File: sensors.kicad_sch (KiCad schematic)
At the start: 2 parts, among them M4 Module-vr-max9924-0.1, M5 Module-knock-0.2

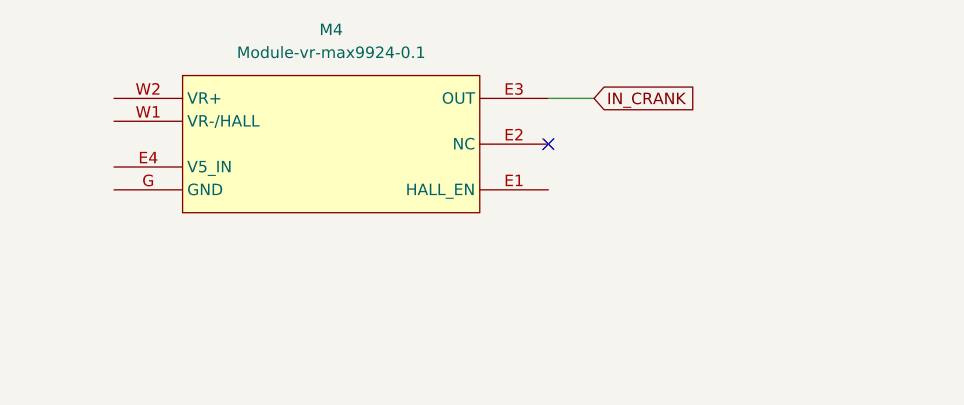
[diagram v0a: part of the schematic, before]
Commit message: Implementing some inputs and outputs
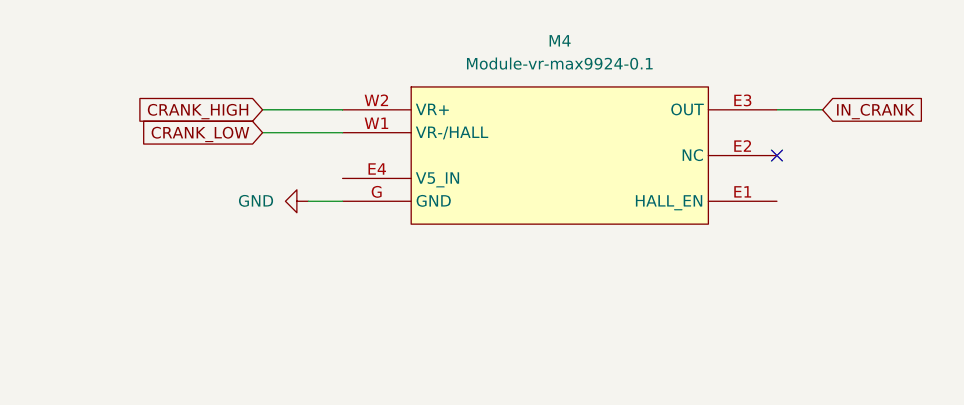
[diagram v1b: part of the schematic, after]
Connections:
- net GND: now also M4.G (GND)
- net CRANK_LOW: now reaches M4.W1 (VR-/HALL)
- net CRANK_HIGH: now reaches M4.W2 (VR+)
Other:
- moved on the sheet: M4
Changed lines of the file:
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@@
 	(paper "A4")
 	(no_connect
-		(at 77.47 46.99)
-	)
-	(wire
-		(pts
-			(xy 77.47 41.91) (xy 82.55 41.91)
+		(at 102.87 48.26)
+	)
+	(wire
+		(pts
+			(xy 102.87 43.18) (xy 107.95 43.18)
+		)
+		(stroke
+			(width 0)
+			(type default)
+		)
+	)
+	(wire
+		(pts
+			(xy 45.72 43.18) (xy 54.61 43.18)
+		)
+		(stroke
+			(width 0)
+			(type default)
+		)
+	)
+	(wire
+		(pts
+			(xy 50.8 53.34) (xy 54.61 53.34)
 		)
 		(stroke
@@
 	(wire
 		(pts
+			(xy 45.72 45.72) (xy 54.61 45.72)
+		)
+		(stroke
+			(width 0)
+			(type default)
+		)
+	)
+	(wire
+		(pts
 			(xy 92.71 120.65) (xy 102.87 120.65)
 		)
@@
 		)
 	)
+	(global_label "CRANK_LOW"
+		(shape input)
+		(at 45.72 45.72 180)
+		(fields_autoplaced yes)
+		(effects
+			(font
+				(size 1.27 1.27)
+			)
+			(justify right)
+		)
+		(property "Intersheetrefs" "${INTERSHEET_REFS}"
+			(at 31.7281 45.72 0)
+			(effects
+				(font
+					(size 1.27 1.27)
+				)
+				(justify right)
+				(hide yes)
+			)
+		)
+	)
 	(global_label "RAW_KNOCK"
 		(shape input)
@@
 	(global_label "IN_CRANK"
 		(shape input)
-		(at 82.55 41.91 0)
+		(at 107.95 43.18 0)
 		(fields_autoplaced yes)
 		(effects
@@
 		)
 		(property "Intersheetrefs" "${INTERSHEET_REFS}"
-			(at 94.6672 41.91 0)
+			(at 120.0672 43.18 0)
 			(effects
 				(font
@@
 				)
 				(justify left)
+				(hide yes)
+			)
+		)
+	)
+	(global_label "CRANK_HIGH"
+		(shape input)
+		(at 45.72 43.18 180)
+		(fields_autoplaced yes)
+		(effects
+			(font
+				(size 1.27 1.27)
+			)
+			(justify right)
+		)
+		(property "Intersheetrefs" "${INTERSHEET_REFS}"
+			(at 31.0023 43.18 0)
+			(effects
+				(font
+					(size 1.27 1.27)
+				)
+				(justify right)
 				(hide yes)
 			)
@@
 	(symbol
 		(lib_id "vr-max9924:Module-vr-max9924-0.1")
-		(at 36.83 39.37 0)
+		(at 62.23 40.64 0)
 		(unit 1)
 		(exclude_from_sim no)
@@
 		(fields_autoplaced yes)
 		(property "Reference" "M4"
-			(at 53.34 34.29 0)
+			(at 78.74 35.56 0)
 			(effects
 				(font
@@
 		)
 		(property "Value" "Module-vr-max9924-0.1"
-			(at 53.34 36.83 0)
+			(at 78.74 38.1 0)
 			(effects
 				(font
@@
 		)
 		(property "Footprint" "0.3:vr-max9924"
-			(at 62.23 38.1 0)
+			(at 87.63 39.37 0)
 			(effects
 				(font
@@
 		)
 		(property "Datasheet" ""
-			(at 36.83 39.37 0)
+			(at 62.23 40.64 0)
 			(effects
 				(font
@@
 		)
 		(property "Description" ""
-			(at 36.83 39.37 0)
+			(at 62.23 40.64 0)
 			(effects
 				(font
@@
 					(unit 1)
 				)
+			)
+		)
+	)
+	(symbol
+		(lib_id "power:GND")
+		(at 50.8 53.34 270)
+		(unit 1)
+		(exclude_from_sim no)
+		(in_bom yes)
+		(on_board yes)
+		(dnp no)
+		(fields_autoplaced yes)
+		(property "Reference" "#PWR023"
+			(at 44.45 53.34 0)
+			(effects
+				(font
+					(size 1.27 1.27)
+				)
+				(hide yes)
+			)
+		)
+		(property "Value" "GND"
+			(at 46.99 53.3399 90)
+			(effects
+				(font
+					(size 1.27 1.27)
+				)
+				(justify right)
+			)
+		)
+		(property "Footprint" ""
+			(at 50.8 53.34 0)
+			(effects
+				(font
+					(size 1.27 1.27)
+				)
+				(hide yes)
+			)
+		)
+		(property "Datasheet" ""
+			(at 50.8 53.34 0)
+			(effects
+				(font
+					(size 1.27 1.27)
+				)
+				(hide yes)
+			)
+		)
+		(property "Description" "Power symbol creates a global label with name \"GND\" , ground"
+			(at 50.8 53.34 0)
+			(effects
+				(font
+					(size 1.27 1.27)
+				)
+				(hide yes)
+			)
+		)
+		(pin "1"
+		)
+		(instances
+			(project ""
+				(path "/83409e39-90d0-4c85-be2e-bd292bea7c12/c21a1b91-ddb8-4e22-b099-7bd7440ec482"
+					(reference "#PWR023")
+					(unit 1)
+				)

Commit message: trying out a layout and routing
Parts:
- added M6: Module-knock-0.2, hellen_knock:knock, symbol knock:Module-knock-0.2
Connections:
- net GND: now also M6.E2 (GND)
- net MCU_KNOCK renamed MCU_KNOCK_F
- net RAW_KNOCK renamed RAW_KNOCK_F
- new net MCU_KNOCK_R: M6.E3 (OUT_KNOCK)
- new net RAW_KNOCK_R: M6.W1 (IN_KNOCK)
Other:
- moved on the sheet: M5

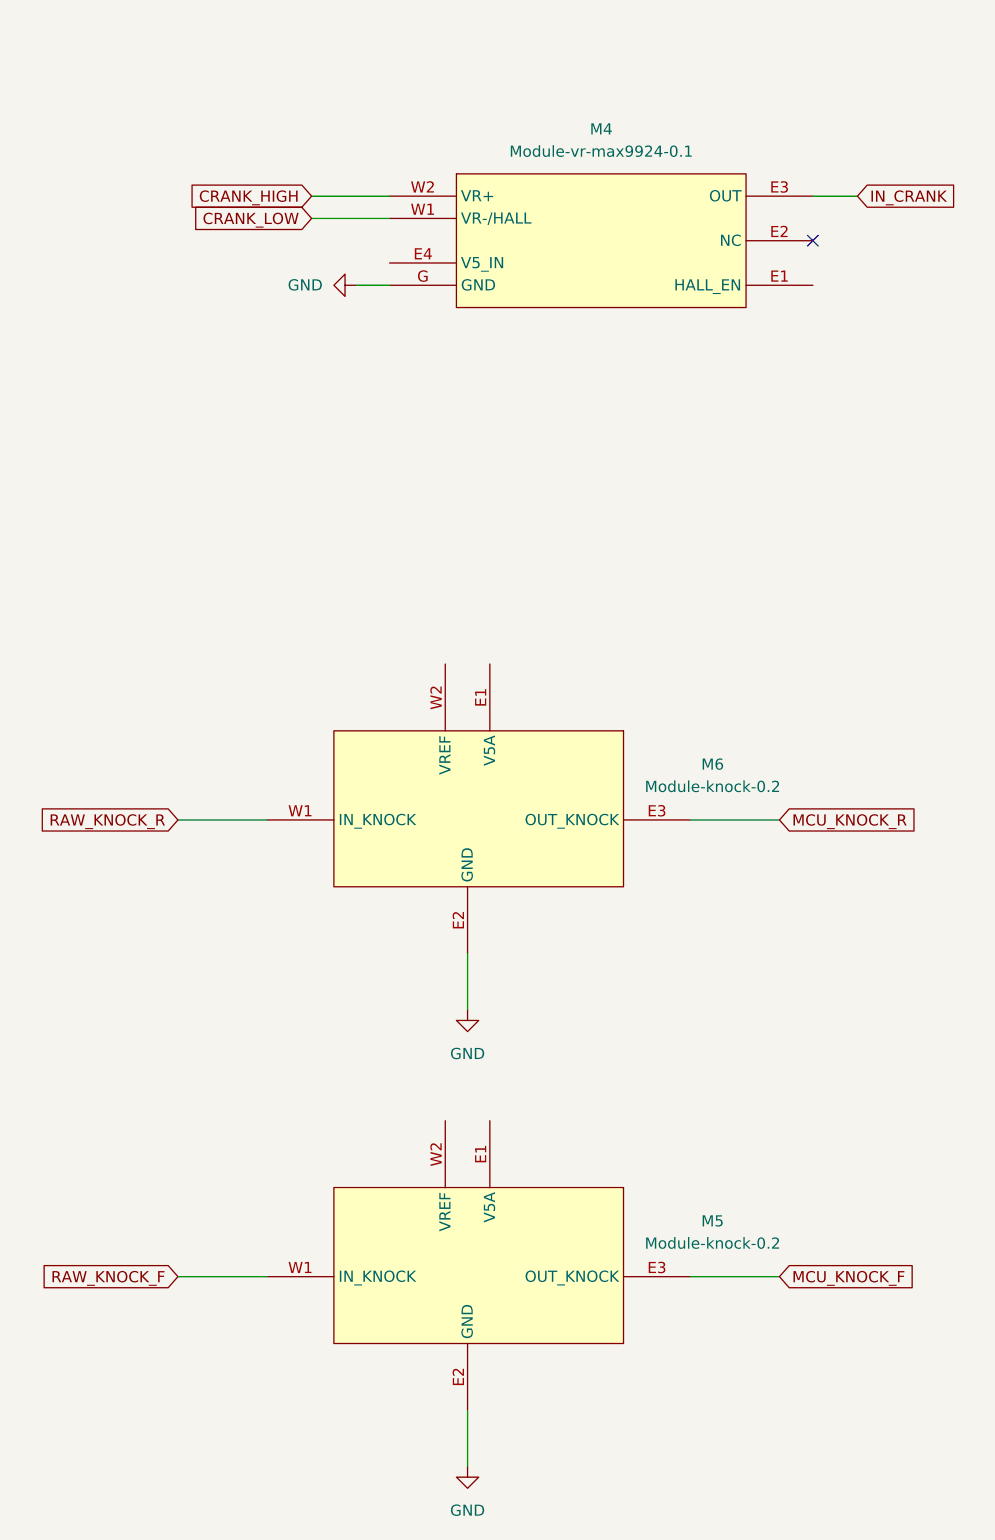
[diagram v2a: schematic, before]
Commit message: adding most remaining outputs and sensors like vvt, cam etc
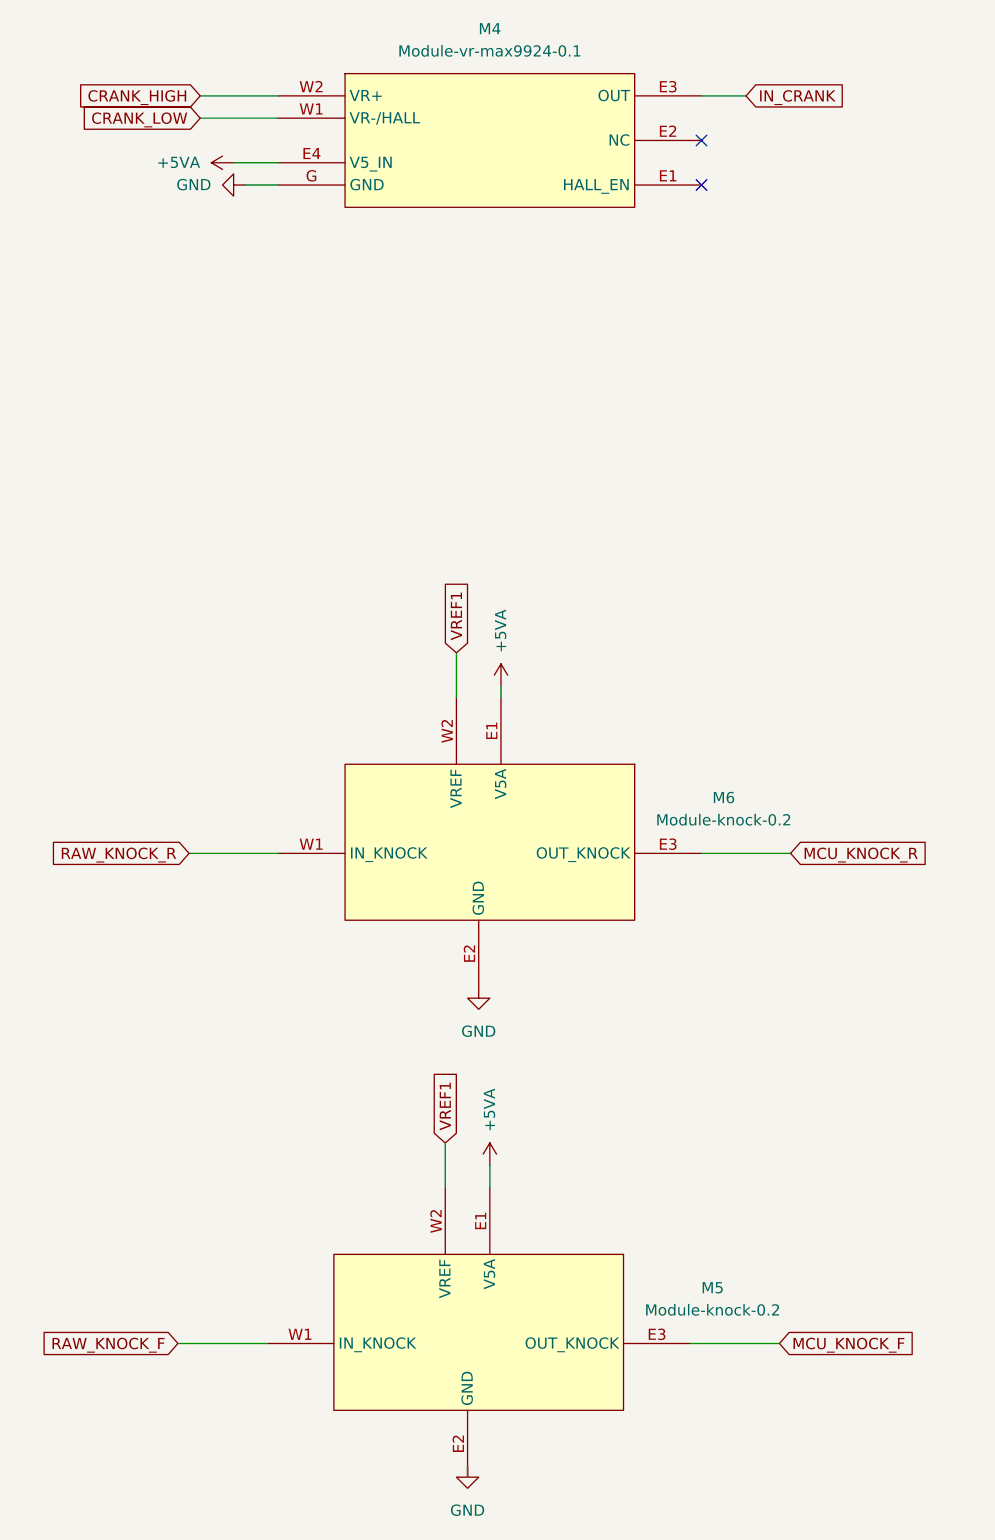
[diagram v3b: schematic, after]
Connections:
- net +5VA: now reaches M5.E1 (V5A)
- net +5VA: now also M4.E4 (V5_IN), M6.E1 (V5A)
- net VREF1: now reaches M5.W2 (VREF)
- net VREF1: now also M6.W2 (VREF)
- no-connect marks 1 -> 2
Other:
- moved on the sheet: M4, M5, M6

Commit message: redone layout, possibly feature complete
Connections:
- net VREF1: no longer M6.W2 (VREF)
- new net VREF2: M6.W2 (VREF)
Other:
- moved on the sheet: M5, M6
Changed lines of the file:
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@@
 	(wire
 		(pts
-			(xy 90.17 118.11) (xy 100.33 118.11)
+			(xy 90.17 96.52) (xy 100.33 96.52)
 		)
 		(stroke
@@
 	(wire
 		(pts
-			(xy 60.96 151.13) (xy 60.96 156.21)
-		)
-		(stroke
-			(width 0)
-			(type default)
-		)
-	)
-	(wire
-		(pts
-			(xy 41.91 118.11) (xy 31.75 118.11)
+			(xy 60.96 139.7) (xy 60.96 144.78)
+		)
+		(stroke
+			(width 0)
+			(type default)
+		)
+	)
+	(wire
+		(pts
+			(xy 41.91 96.52) (xy 31.75 96.52)
 		)
 		(stroke
@@
 	(wire
 		(pts
-			(xy 40.64 173.99) (xy 30.48 173.99)
-		)
-		(stroke
-			(width 0)
-			(type default)
-		)
-	)
-	(wire
-		(pts
-			(xy 63.5 189.23) (xy 63.5 187.96)
-		)
-		(stroke
-			(width 0)
-			(type default)
-		)
-	)
-	(wire
-		(pts
-			(xy 67.31 100.33) (xy 67.31 99.06)
+			(xy 40.64 162.56) (xy 30.48 162.56)
+		)
+		(stroke
+			(width 0)
+			(type default)
+		)
+	)
+	(wire
+		(pts
+			(xy 63.5 177.8) (xy 63.5 176.53)
+		)
+		(stroke
+			(width 0)
+			(type default)
+		)
+	)
+	(wire
+		(pts
+			(xy 67.31 78.74) (xy 67.31 77.47)
 		)
 		(stroke
@@
 	(wire
 		(pts
-			(xy 62.23 95.25) (xy 62.23 100.33)
-		)
-		(stroke
-			(width 0)
-			(type default)
-		)
-	)
-	(wire
-		(pts
-			(xy 88.9 173.99) (xy 99.06 173.99)
-		)
-		(stroke
-			(width 0)
-			(type default)
-		)
-	)
-	(wire
-		(pts
-			(xy 66.04 156.21) (xy 66.04 153.67)
+			(xy 62.23 73.66) (xy 62.23 78.74)
+		)
+		(stroke
+			(width 0)
+			(type default)
+		)
+	)
+	(wire
+		(pts
+			(xy 88.9 162.56) (xy 99.06 162.56)
+		)
+		(stroke
+			(width 0)
+			(type default)
+		)
+	)
+	(wire
+		(pts
+			(xy 66.04 144.78) (xy 66.04 142.24)
 		)
 		(stroke
@@
 	(global_label "RAW_KNOCK_R"
 		(shape input)
-		(at 31.75 118.11 180)
+		(at 31.75 96.52 180)
 		(fields_autoplaced yes)
 		(effects
@@
 		)
 		(property "Intersheetrefs" "${INTERSHEET_REFS}"
-			(at 15.2786 118.11 0)
+			(at 15.2786 96.52 0)
 			(effects
 				(font
@@
 	(global_label "MCU_KNOCK_R"
 		(shape input)
-		(at 100.33 118.11 0)
+		(at 100.33 96.52 0)
 		(fields_autoplaced yes)
 		(effects
@@
 		)
 		(property "Intersheetrefs" "${INTERSHEET_REFS}"
-			(at 117.0433 118.11 0)
+			(at 117.0433 96.52 0)
 			(effects
 				(font
@@
 	(global_label "RAW_KNOCK_F"
 		(shape input)
-		(at 30.48 173.99 180)
+		(at 30.48 162.56 180)
 		(fields_autoplaced yes)
 		(effects
@@
 		)
 		(property "Intersheetrefs" "${INTERSHEET_REFS}"
-			(at 14.19 173.99 0)
+			(at 14.19 162.56 0)
 			(effects
 				(font
@@
 		)
 	)
-	(global_label "VREF1"
+	(global_label "VREF2"
 		(shape input)
-		(at 62.23 95.25 90)
+		(at 62.23 73.66 90)
 		(fields_autoplaced yes)
 		(effects
@@
 		)
 		(property "Intersheetrefs" "${INTERSHEET_REFS}"
-			(at 62.23 86.4591 90)
+			(at 62.23 64.8691 90)
 			(effects
 				(font
@@
 	(global_label "VREF1"
 		(shape input)
-		(at 60.96 151.13 90)
+		(at 60.96 139.7 90)
 		(fields_autoplaced yes)
 		(effects
@@
 		)
 		(property "Intersheetrefs" "${INTERSHEET_REFS}"
-			(at 60.96 142.3391 90)
+			(at 60.96 130.9091 90)
 			(effects
 				(font
@@
 	(global_label "MCU_KNOCK_F"
 		(shape input)
-		(at 99.06 173.99 0)
+		(at 99.06 162.56 0)
 		(fields_autoplaced yes)
 		(effects
@@
 		)
 		(property "Intersheetrefs" "${INTERSHEET_REFS}"
-			(at 115.5919 173.99 0)
+			(at 115.5919 162.56 0)
 			(effects
 				(font
@@
 	(symbol
 		(lib_id "power:+5VA")
-		(at 67.31 99.06 0)
+		(at 67.31 77.47 0)
 		(unit 1)
 		(exclude_from_sim no)
@@
 		(fields_autoplaced yes)
 		(property "Reference" "#PWR061"
-			(at 67.31 102.87 0)
+			(at 67.31 81.28 0)
 			(effects
 				(font
@@
 		)
 		(property "Value" "+5VA"
-			(at 67.3099 95.25 90)
+			(at 67.3099 73.66 90)
 			(effects
 				(font
@@
 		)
 		(property "Footprint" ""
-			(at 67.31 99.06 0)
+			(at 67.31 77.47 0)
 			(effects
 				(font
@@
 		)
 		(property "Datasheet" ""
-			(at 67.31 99.06 0)
+			(at 67.31 77.47 0)
 			(effects
 				(font
@@
 		)
 		(property "Description" "Power symbol creates a global label with name \"+5VA\""
-			(at 67.31 99.06 0)
+			(at 67.31 77.47 0)
 			(effects
 				(font
@@
 	(symbol
 		(lib_id "knock:Module-knock-0.2")
-		(at 48.26 163.83 0)
+		(at 48.26 152.4 0)
 		(unit 1)
 		(exclude_from_sim no)
@@
 		(fields_autoplaced yes)
 		(property "Reference" "M5"
-			(at 91.44 167.6714 0)
+			(at 91.44 156.2414 0)
 			(effects
 				(font
@@
 		)
 		(property "Value" "Module-knock-0.2"
-			(at 91.44 170.2114 0)
+			(at 91.44 158.7814 0)
 			(effects
 				(font
@@
 		)
 		(property "Footprint" "hellen_knock:knock"
-			(at 64.008 170.434 0)
+			(at 64.008 159.004 0)
 			(effects
 				(font
@@
 		)
 		(property "Datasheet" ""
-			(at 48.26 163.83 0)
+			(at 48.26 152.4 0)
 			(effects
 				(font
@@
 		)
 		(property "Description" "Hellen-One Knock Pre-amplifier Module"
-			(at 86.868 162.052 0)
+			(at 86.868 150.622 0)
 			(effects
 				(font
@@
 	(symbol
 		(lib_id "knock:Module-knock-0.2")
-		(at 49.53 107.95 0)
+		(at 49.53 86.36 0)
 		(unit 1)
 		(exclude_from_sim no)
@@
 		(fields_autoplaced yes)
 		(property "Reference" "M6"
-			(at 92.71 111.7914 0)
+			(at 92.71 90.2014 0)
 			(effects
 				(font
@@
 		)
 		(property "Value" "Module-knock-0.2"
-			(at 92.71 114.3314 0)
+			(at 92.71 92.7414 0)
 			(effects
 				(font
@@
 		)
 		(property "Footprint" "hellen_knock:knock"
-			(at 65.278 114.554 0)
+			(at 65.278 92.964 0)
 			(effects
 				(font
@@
 		)
 		(property "Datasheet" ""
-			(at 49.53 107.95 0)
+			(at 49.53 86.36 0)
 			(effects
 				(font
@@
 		)
 		(property "Description" "Hellen-One Knock Pre-amplifier Module"
-			(at 88.138 106.172 0)
+			(at 88.138 84.582 0)
 			(effects
 				(font
@@
 	(symbol
 		(lib_id "power:GND")
-		(at 64.77 133.35 0)
+		(at 64.77 111.76 0)
 		(unit 1)
 		(exclude_from_sim no)
@@
 		(fields_autoplaced yes)
 		(property "Reference" "#PWR046"
-			(at 64.77 139.7 0)
+			(at 64.77 118.11 0)
 			(effects
 				(font
@@
 		)
 		(property "Value" "GND"
-			(at 64.77 138.43 0)
+			(at 64.77 116.84 0)
 			(effects
 				(font
@@
 		)
 		(property "Footprint" ""
-			(at 64.77 133.35 0)
+			(at 64.77 111.76 0)
 			(effects
 				(font
@@
 		)
 		(property "Datasheet" ""
-			(at 64.77 133.35 0)
+			(at 64.77 111.76 0)
 			(effects
 				(font
@@
 		)
 		(property "Description" "Power symbol creates a global label with name \"GND\" , ground"
-			(at 64.77 133.35 0)
+			(at 64.77 111.76 0)
 			(effects
 				(font
@@
 	(symbol
 		(lib_id "power:GND")
-		(at 63.5 187.96 0)
+		(at 63.5 176.53 0)
 		(unit 1)
 		(exclude_from_sim no)
@@
 		(fields_autoplaced yes)
 		(property "Reference" "#PWR021"
-			(at 63.5 194.31 0)
+			(at 63.5 182.88 0)
 			(effects
 				(font
@@
 		)
 		(property "Value" "GND"
-			(at 63.5 193.04 0)
+			(at 63.5 181.61 0)
 			(effects
 				(font
@@
 		)
 		(property "Footprint" ""
-			(at 63.5 187.96 0)
+			(at 63.5 176.53 0)
 			(effects
 				(font
@@
 		)
 		(property "Datasheet" ""
-			(at 63.5 187.96 0)
+			(at 63.5 176.53 0)
 			(effects
 				(font
@@
 		)
 		(property "Description" "Power symbol creates a global label with name \"GND\" , ground"
-			(at 63.5 187.96 0)
+			(at 63.5 176.53 0)
 			(effects
 				(font
@@
 	(symbol
 		(lib_id "power:+5VA")
-		(at 66.04 153.67 0)
+		(at 66.04 142.24 0)
 		(unit 1)
 		(exclude_from_sim no)
@@
 		(fields_autoplaced yes)
 		(property "Reference" "#PWR062"
-			(at 66.04 157.48 0)
+			(at 66.04 146.05 0)
 			(effects
 				(font
@@
 		)
 		(property "Value" "+5VA"
-			(at 66.0399 149.86 90)
+			(at 66.0399 138.43 90)
 			(effects
 				(font
@@
 		)
 		(property "Footprint" ""
-			(at 66.04 153.67 0)
+			(at 66.04 142.24 0)
 			(effects
 				(font
@@
 		)
 		(property "Datasheet" ""
-			(at 66.04 153.67 0)
+			(at 66.04 142.24 0)
 			(effects
 				(font
@@
 		)
 		(property "Description" "Power symbol creates a global label with name \"+5VA\""
-			(at 66.04 153.67 0)
-			(effects
-				(font
+			(at 66.04 142.24 0)
+			(effects
+				(font
